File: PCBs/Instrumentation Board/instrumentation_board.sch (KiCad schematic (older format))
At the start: 24 parts, among them J1 Conn_01x02, J2 Conn_01x02, Q1 Q_Photo_NPN, U2 LSM6DS3HTR, U3 LSM6DS3HTR, U4 MicroSDBreakout, U5 GPS, U7 MS5607-02BA03

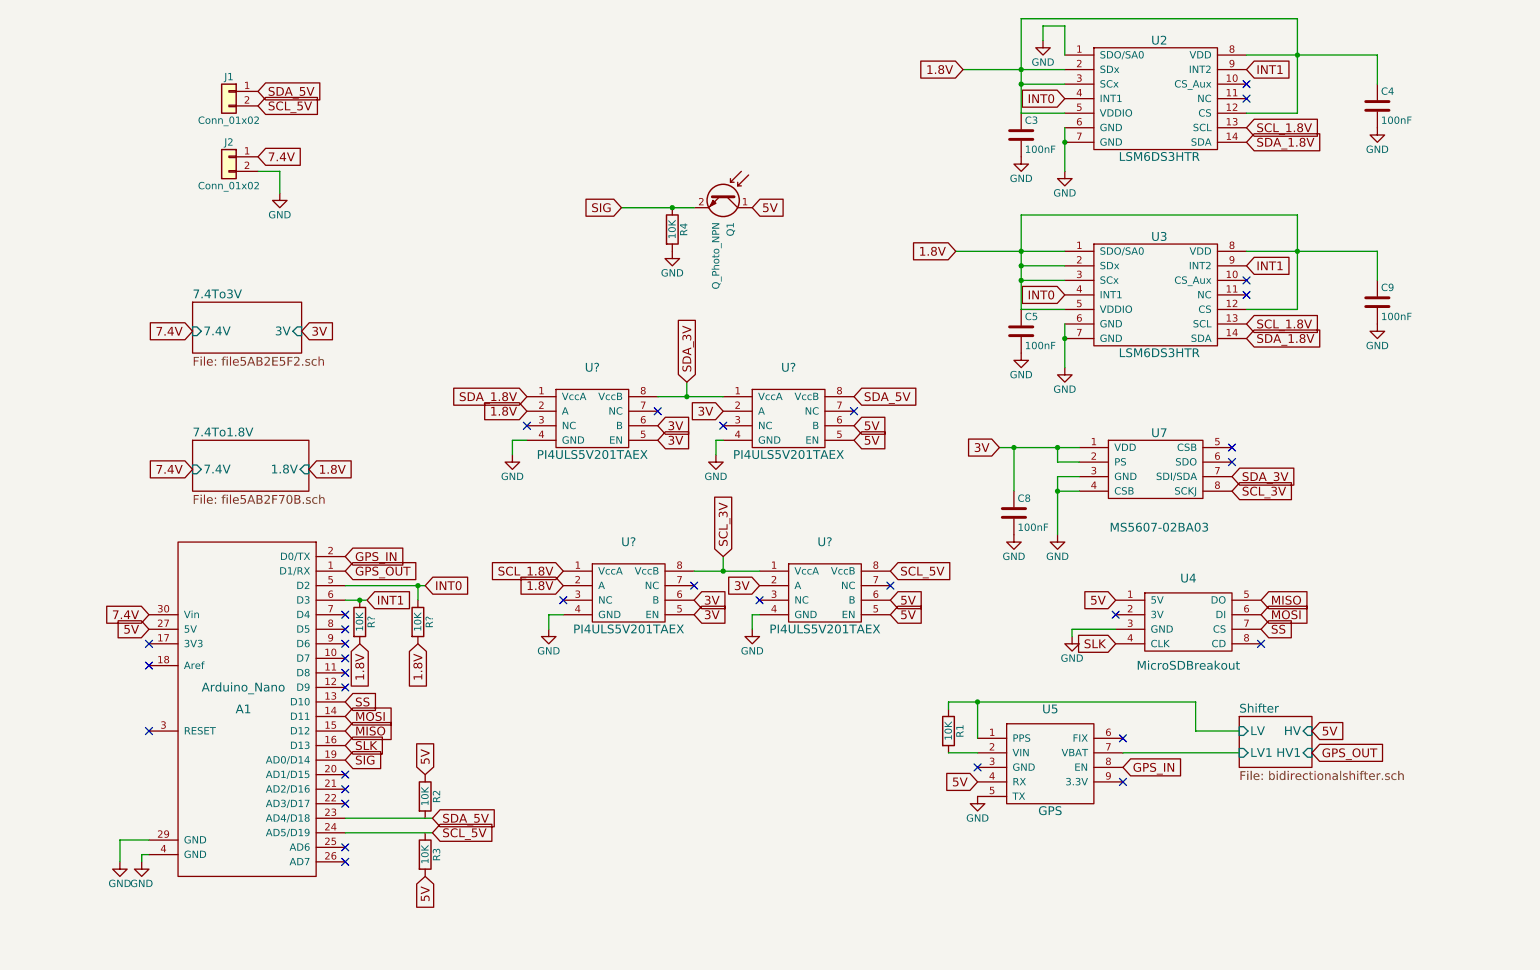
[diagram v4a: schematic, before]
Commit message: fixed swapped pins
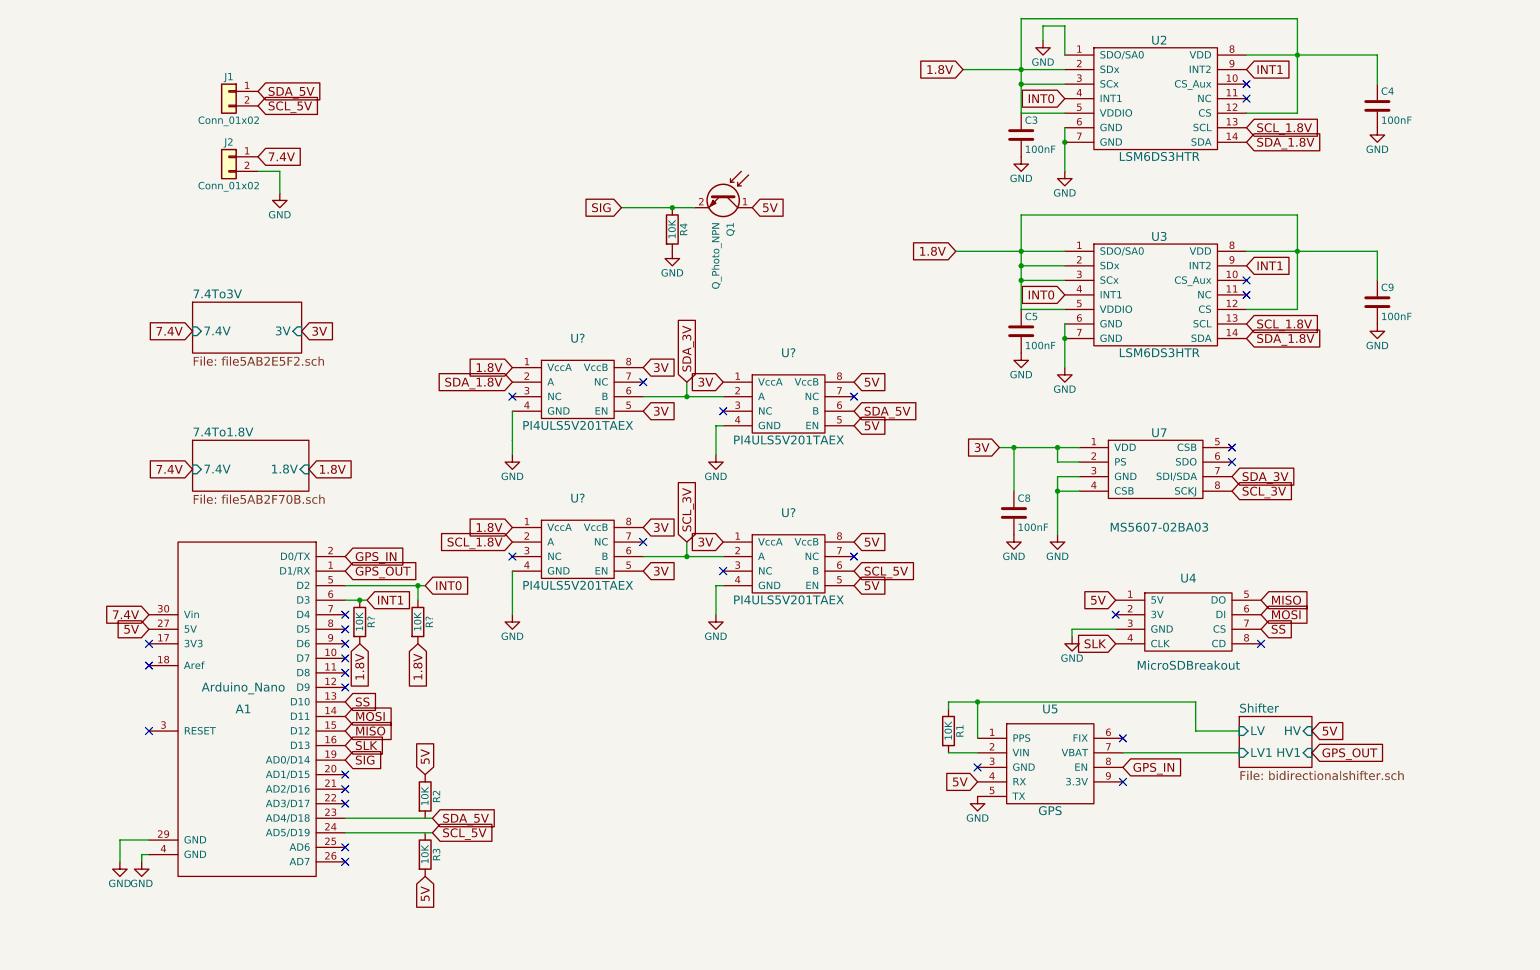
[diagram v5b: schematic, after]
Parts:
- removed U? (x2): PI4ULS5V201TAEX, symbol PI4ULS5V201TAEX
- added U? (x2): PI4ULS5V201TAEX, symbol PI4ULS5V201TAEX
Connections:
- net 1.8V: now also U?.1 (VccA), U?.1 (VccA); no longer U?.2 (A)
- net 3V: now also U?.1 (VccA), U?.8 (VccB), U?.1 (VccA), U?.5 (EN), U?.8 (VccB); no longer U?.2 (A), U?.6 (B)
- net 5V: now also U?.8 (VccB), U?.5 (EN), U?.8 (VccB); no longer U?.6 (B)
- net GND: now also U?.4 (GND), U?.4 (GND)
- net SCL_1.8V: now also U?.2 (A)
- net SCL_3V: now also U?.2 (A), U?.6 (B)
- net SCL_5V: now also U?.6 (B)
- net SDA_1.8V: now also U?.2 (A); no longer U?.1 (VccA)
- net SDA_3V: now also U?.2 (A), U?.6 (B); no longer U?.1 (VccA), U?.8 (VccB)
- net SDA_5V: now also U?.6 (B); no longer U?.8 (VccB)
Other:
- moved on the sheet: U?
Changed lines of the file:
@@
 L PI4ULS5V201TAEX U?
 U 1 1 5AB5D648
-P 5850 3750
-F 0 "U?" H 5850 4300 60  0000 C CNN
-F 1 "PI4ULS5V201TAEX" H 5850 3700 60  0000 C CNN
-F 2 "" H 5850 3750 60  0001 C CNN
-F 3 "" H 5850 3750 60  0001 C CNN
-	1    5850 3750
-	1    0    0    -1
-$EndComp
-Text GLabel 6300 3600 2    60   Input ~ 0
+P 5850 3650
+F 0 "U?" H 5850 4200 60  0000 C CNN
+F 1 "PI4ULS5V201TAEX" H 5850 3600 60  0000 C CNN
+F 2 "" H 5850 3650 60  0001 C CNN
+F 3 "" H 5850 3650 60  0001 C CNN
+	1    5850 3650
+	1    0    0    -1
+$EndComp
+Text GLabel 6300 3300 2    60   Input ~ 0
 5V
-Text GLabel 6300 3400 2    60   Input ~ 0
+Text GLabel 6300 3500 2    60   Input ~ 0
 SDA_5V
-Text GLabel 5400 3500 0    60   Input ~ 0
+Text GLabel 5400 3300 0    60   Input ~ 0
 3V
 Text GLabel 5150 3300 1    60   Input ~ 0
 SDA_3V
-Text GLabel 6300 3700 2    60   Input ~ 0
+Text GLabel 6300 3600 2    60   Input ~ 0
 5V
 $Comp
@@
 L PI4ULS5V201TAEX U?
 U 1 1 5AB67DF3
-P 4500 3750
-F 0 "U?" H 4500 4300 60  0000 C CNN
-F 1 "PI4ULS5V201TAEX" H 4500 3700 60  0000 C CNN
-F 2 "" H 4500 3750 60  0001 C CNN
-F 3 "" H 4500 3750 60  0001 C CNN
-	1    4500 3750
+P 4400 3550
+F 0 "U?" H 4400 4100 60  0000 C CNN
+F 1 "PI4ULS5V201TAEX" H 4400 3500 60  0000 C CNN
+F 2 "" H 4400 3550 60  0001 C CNN
+F 3 "" H 4400 3550 60  0001 C CNN
+	1    4400 3550
 	1    0    0    -1
 $EndComp
@@
 	7150 5500 7150 5750
 Wire Wire Line
-	6950 5500 8650 5500
-Wire Wire Line
-	7000 2400 7750 2400
+	6950 5500 7150 5500
+Wire Wire Line
+	7150 5500 8650 5500
+Wire Wire Line
+	7000 2400 7450 2400
+Wire Wire Line
+	7450 2400 7750 2400
 Wire Wire Line
 	7600 850  7600 950
@@
 Connection ~ 7750 3000
 Wire Wire Line
-	7750 2900 7750 3200
+	7750 2900 7750 3000
+Wire Wire Line
+	7750 3000 7750 3200
 Wire Wire Line
 	9350 2800 9000 2800
@@
 	7450 2800 7750 2800
 Wire Wire Line
-	9000 2400 9900 2400
-Wire Wire Line
-	9350 2150 9350 2800
+	9000 2400 9350 2400
+Wire Wire Line
+	9350 2400 9900 2400
+Wire Wire Line
+	9350 2150 9350 2400
+Wire Wire Line
+	9350 2400 9350 2800
 Wire Wire Line
 	7450 2150 9350 2150
 Wire Wire Line
-	7450 2150 7450 2800
+	7450 2150 7450 2400
+Wire Wire Line
+	7450 2400 7450 2500
+Wire Wire Line
+	7450 2500 7450 2600
+Wire Wire Line
+	7450 2600 7450 2800
 Connection ~ 7450 1250
 Wire Wire Line
@@
 Connection ~ 7450 1150
 Wire Wire Line
-	7050 1150 7750 1150
+	7050 1150 7450 1150
+Wire Wire Line
+	7450 1150 7750 1150
 Connection ~ 7750 1650
 Wire Wire Line
-	7750 1550 7750 1850
+	7750 1550 7750 1650
+Wire Wire Line
+	7750 1650 7750 1850
 Wire Wire Line
 	9350 1450 9000 1450
@@
 	7450 1450 7750 1450
 Wire Wire Line
-	9000 1050 9900 1050
-Wire Wire Line
-	9350 800  9350 1450
+	9000 1050 9350 1050
+Wire Wire Line
+	9350 1050 9900 1050
+Wire Wire Line
+	9350 800  9350 1050
+Wire Wire Line
+	9350 1050 9350 1450
 Wire Wire Line
 	7450 800  9350 800
 Wire Wire Line
-	7450 800  7450 1450
+	7450 800  7450 1150
+Wire Wire Line
+	7450 1150 7450 1250
+Wire Wire Line
+	7450 1250 7450 1450
 Wire Wire Line
 	7800 5000 8100 5000
@@
 	7850 4050 7700 4050
 Wire Wire Line
-	7700 3950 7700 4350
+	7700 3950 7700 4050
+Wire Wire Line
+	7700 4050 7700 4350
 Wire Wire Line
 	7850 3950 7700 3950
@@
 	7400 3750 7400 4050
 Wire Wire Line
-	7300 3750 7850 3750
+	7300 3750 7400 3750
+Wire Wire Line
+	7400 3750 7700 3750
+Wire Wire Line
+	7700 3750 7850 3750
 Wire Wire Line
 	1250 6450 1450 6450
@@
 	2800 6400 3400 6400
 Wire Wire Line
-	4700 2100 5200 2100
+	4700 2100 5050 2100
+Wire Wire Line
+	5050 2100 5200 2100
 Connection ~ 5050 2100
 Wire Wire Line
-	5350 3800 5350 3700
-Wire Wire Line
-	5350 3700 5400 3700
-Wire Wire Line
-	4950 3400 5400 3400
+	5350 3800 5350 3600
+Wire Wire Line
+	5350 3600 5400 3600
+Wire Wire Line
+	4850 3400 5150 3400
+Wire Wire Line
+	5150 3400 5400 3400
 Wire Wire Line
 	5150 3400 5150 3300
 Connection ~ 5150 3400
-NoConn ~ 6300 3500
-NoConn ~ 5400 3600
-Text GLabel 4950 3600 2    60   Input ~ 0
-3V
-Text GLabel 4950 3700 2    60   Input ~ 0
-3V
-NoConn ~ 4950 3500
-NoConn ~ 4050 3600
-Text GLabel 4050 3500 0    60   Input ~ 0
+NoConn ~ 6300 3400
+NoConn ~ 5400 3500
+Text GLabel 4850 3200 2    60   Input ~ 0
+3V
+Text GLabel 4850 3500 2    60   Input ~ 0
+3V
+NoConn ~ 4850 3300
+NoConn ~ 3950 3400
+Text GLabel 3950 3200 0    60   Input ~ 0
 1.8V
-Text GLabel 4050 3400 0    60   Input ~ 0
+Text GLabel 3950 3300 0    60   Input ~ 0
 SDA_1.8V
-$Comp
-L PI4ULS5V201TAEX U?
-U 1 1 5AB6A1B5
-P 6100 4950
-F 0 "U?" H 6100 5500 60  0000 C CNN
-F 1 "PI4ULS5V201TAEX" H 6100 4900 60  0000 C CNN
-F 2 "" H 6100 4950 60  0001 C CNN
-F 3 "" H 6100 4950 60  0001 C CNN
-	1    6100 4950
-	1    0    0    -1
-$EndComp
-Text GLabel 6550 4800 2    60   Input ~ 0
-5V
-Text GLabel 5650 4700 0    60   Input ~ 0
-3V
-Text GLabel 6550 4900 2    60   Input ~ 0
-5V
-$Comp
-L GND #PWR?
-U 1 1 5AB6A1C0
-P 5600 5000
-F 0 "#PWR?" H 5600 4750 50  0001 C CNN
-F 1 "GND" H 5600 4850 50  0000 C CNN
-F 2 "" H 5600 5000 50  0001 C CNN
-F 3 "" H 5600 5000 50  0001 C CNN
-	1    5600 5000
-	1    0    0    -1
-$EndComp
-$Comp
-L PI4ULS5V201TAEX U?
-U 1 1 5AB6A1C6
-P 4750 4950
-F 0 "U?" H 4750 5500 60  0000 C CNN
-F 1 "PI4ULS5V201TAEX" H 4750 4900 60  0000 C CNN
-F 2 "" H 4750 4950 60  0001 C CNN
-F 3 "" H 4750 4950 60  0001 C CNN
-	1    4750 4950
-	1    0    0    -1
-$EndComp
-Wire Wire Line
-	5600 5000 5600 4900
-Wire Wire Line
-	5600 4900 5650 4900
-Wire Wire Line
-	5200 4600 5650 4600
-Wire Wire Line
-	5400 4600 5400 4500
-Connection ~ 5400 4600
-NoConn ~ 6550 4700
-NoConn ~ 5650 4800
-Text GLabel 5200 4800 2    60   Input ~ 0
-3V
-Text GLabel 5200 4900 2    60   Input ~ 0
-3V
-NoConn ~ 5200 4700
-NoConn ~ 4300 4800
-Text GLabel 4300 4700 0    60   Input ~ 0
-1.8V
 $Comp
 L GND #PWR?
@@
 	1    0    0    -1
 $EndComp
-$Comp
-L GND #PWR?
-U 1 1 5AB6A36E
-P 4200 5000
-F 0 "#PWR?" H 4200 4750 50  0001 C CNN
-F 1 "GND" H 4200 4850 50  0000 C CNN
-F 2 "" H 4200 5000 50  0001 C CNN
-F 3 "" H 4200 5000 50  0001 C CNN
-	1    4200 5000
-	1    0    0    -1
-$EndComp
 Wire Wire Line
 	3950 3800 3950 3700
 Wire Wire Line
-	3950 3700 4050 3700
-Wire Wire Line
-	4200 5000 4200 4900
-Wire Wire Line
-	4200 4900 4300 4900
-Text GLabel 6550 4600 2    60   Input ~ 0
+	3950 3700 3950 3500
+Text GLabel 6300 4600 2    60   Input ~ 0
 SCL_5V
-Text GLabel 5400 4500 1    60   Input ~ 0
+Text GLabel 5150 4400 1    60   Input ~ 0
 SCL_3V
-Text GLabel 4300 4600 0    60   Input ~ 0
+Text GLabel 3950 4400 0    60   Input ~ 0
 SCL_1.8V
 Text GLabel 2900 5100 3    60   Input ~ 0
@@
 $EndComp
 Wire Wire Line
-	2800 4700 3350 4700
+	2800 4700 3300 4700
+Wire Wire Line
+	3300 4700 3350 4700
 Wire Wire Line
 	3300 4700 3300 4800
 Connection ~ 3300 4700
 Wire Wire Line
-	2800 4800 2950 4800
+	2800 4800 2900 4800
+Wire Wire Line
+	2900 4800 2950 4800
 Connection ~ 2900 4800
+$Comp
+L PI4ULS5V201TAEX U?
+U 1 1 5AB6EE1D
+P 5850 4750
+F 0 "U?" H 5850 5300 60  0000 C CNN
+F 1 "PI4ULS5V201TAEX" H 5850 4700 60  0000 C CNN
+F 2 "" H 5850 4750 60  0001 C CNN
+F 3 "" H 5850 4750 60  0001 C CNN
+	1    5850 4750
+	1    0    0    -1
+$EndComp
+Text GLabel 6300 4400 2    60   Input ~ 0
+5V
+Text GLabel 5400 4400 0    60   Input ~ 0
+3V
+Text GLabel 6300 4700 2    60   Input ~ 0
+5V
+$Comp
+L GND #PWR?
+U 1 1 5AB6EE28
+P 5350 4900
+F 0 "#PWR?" H 5350 4650 50  0001 C CNN
+F 1 "GND" H 5350 4750 50  0000 C CNN
+F 2 "" H 5350 4900 50  0001 C CNN
+F 3 "" H 5350 4900 50  0001 C CNN
+	1    5350 4900
+	1    0    0    -1
+$EndComp
+$Comp
+L PI4ULS5V201TAEX U?
+U 1 1 5AB6EE2E
+P 4400 4650
+F 0 "U?" H 4400 5200 60  0000 C CNN
+F 1 "PI4ULS5V201TAEX" H 4400 4600 60  0000 C CNN
+F 2 "" H 4400 4650 60  0001 C CNN
+F 3 "" H 4400 4650 60  0001 C CNN
+	1    4400 4650
+	1    0    0    -1
+$EndComp
+Wire Wire Line
+	5350 4900 5350 4700
+Wire Wire Line
+	5350 4700 5400 4700
+Wire Wire Line
+	4850 4500 5150 4500
+Wire Wire Line
+	5150 4500 5400 4500
+Wire Wire Line
+	5150 4500 5150 4400
+Connection ~ 5150 4500
+NoConn ~ 6300 4500
+NoConn ~ 5400 4600
+Text GLabel 4850 4300 2    60   Input ~ 0
+3V
+Text GLabel 4850 4600 2    60   Input ~ 0
+3V
+NoConn ~ 4850 4400
+NoConn ~ 3950 4500
+Text GLabel 3950 4300 0    60   Input ~ 0
+1.8V
+$Comp
+L GND #PWR?
+U 1 1 5AB6EE42
+P 3950 4900
+F 0 "#PWR?" H 3950 4650 50  0001 C CNN
+F 1 "GND" H 3950 4750 50  0000 C CNN
+F 2 "" H 3950 4900 50  0001 C CNN
+F 3 "" H 3950 4900 50  0001 C CNN
+	1    3950 4900
+	1    0    0    -1
+$EndComp
+Wire Wire Line
+	3950 4900 3950 4800
+Wire Wire Line
+	3950 4800 3950 4600
 $EndSCHEMATC

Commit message: changes as per Alex's review
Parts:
- removed R3, R? (x2): 10K, symbol R
- removed U? (x4): PI4ULS5V201TAEX, symbol PI4ULS5V201TAEX
- R1, R2: value 10K -> 0
- U4: value MicroSDBreakout -> MicroSD-ADAFRUIT254
- U5: value GPS -> GPS-ADAFRUIT746
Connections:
- net 5V: no longer R2.1
- net at R1.2: now also A1.5 (D2); no longer U5.2 (VIN)
- net at R2.2: now also A1.6 (D3)
- net INT0 renamed INT0_1.8V
- net INT0_1.8V: no longer A1.5 (D2)
- net INT1 renamed INT1_1.8V
- net INT1_1.8V: no longer A1.6 (D3)
- net Shifter/LV renamed ICShifter/VccA
- net ICShifter/VccA: no longer R1.1
- net Shifter/LV1 renamed ICShifter/A
- new net INT0_5V: R2.1
- new net INT1_5V: R1.1
- no-connect marks 33 -> 25
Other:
- moved on the sheet: C3, C5

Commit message: pinout changes
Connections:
- net 5V: now also U5.2 (VIN); no longer U5.4 (RX)
- net GND: now also U5.3 (GND); no longer U5.5 (TX)
- net GPS_IN: now also U5.4 (RX); no longer U5.8 (EN)
- net ICShifter/A: now also U5.5 (TX); no longer U5.7 (VBAT)
- net ICShifter/VccA: now also U5.9 (3.3V); no longer U5.1 (PPS)
- no-connect marks 25 -> 26
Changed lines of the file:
@@
 LIBS:contrib
 LIBS:valves
+LIBS:a2135-h
+LIBS:ap2204k-5
+LIBS:arduino_nano
+LIBS:fgpmmopa6h
+LIBS:Recovery Board Parts
+LIBS:Recovery Board-cache
+LIBS:sot-223
 LIBS:instrumentation_board_parts
 LIBS:instrumentation_board-cache
@@
 U 1 1 5A9B54D4
 P 7650 6000
-F 0 "U5" H 7650 6450 60  0000 C CNN
+F 0 "U5" H 7650 6500 60  0000 C CNN
 F 1 "GPS-ADAFRUIT746" H 7650 5750 60  0000 C CNN
 F 2 "" H 7750 5900 60  0001 C CNN
@@
 L GND #PWR5
 U 1 1 5A9B5B00
-P 7150 6150
-F 0 "#PWR5" H 7150 5900 50  0001 C CNN
-F 1 "GND" H 7150 6000 50  0000 C CNN
-F 2 "" H 7150 6150 50  0001 C CNN
-F 3 "" H 7150 6150 50  0001 C CNN
-	1    7150 6150
+P 6700 6100
+F 0 "#PWR5" H 6700 5850 50  0001 C CNN
+F 1 "GND" H 6700 5950 50  0000 C CNN
+F 2 "" H 6700 6100 50  0001 C CNN
+F 3 "" H 6700 6100 50  0001 C CNN
+	1    6700 6100
 	1    0    0    -1
 $EndComp
@@
 Text GLabel 2800 4600 2    60   Input ~ 0
 GPS_OUT
-Text GLabel 8150 5950 2    60   Input ~ 0
+Text GLabel 7150 6050 0    60   Input ~ 0
 GPS_IN
-Text GLabel 9650 5850 2    60   Input ~ 0
+Text GLabel 9650 6000 2    60   Input ~ 0
 GPS_OUT
 $Comp
@@
 Text GLabel 1450 5000 0    60   Input ~ 0
 5V
-Text GLabel 7150 6050 0    60   Input ~ 0
+Text GLabel 7150 5850 0    60   Input ~ 0
 5V
 Text GLabel 8100 4800 0    60   Input ~ 0
@@
 NoConn ~ 9100 5100
 NoConn ~ 8150 5750
-NoConn ~ 7150 5950
-NoConn ~ 8150 6050
 NoConn ~ 8900 3750
 NoConn ~ 8900 3850
@@
 F0 "ICShifter" 60
 F1 "Shifter.sch" 60
-F2 "B" I R 9650 5850 60
-F3 "VccB" I R 9650 6000 60
-F4 "A" I L 8950 5850 60
-F5 "VccA" I L 8950 6000 60
+F2 "B" I R 9650 6000 60
+F3 "VccB" I R 9650 5850 60
+F4 "A" I L 8950 6000 60
+F5 "VccA" I L 8950 5850 60
 $EndSheet
 $Sheet
@@
 	0    1    1    0
 $EndComp
-Text GLabel 9650 6000 2    60   Input ~ 0
+Text GLabel 9650 5850 2    60   Input ~ 0
 5V
 Connection ~ 7700 3750
@@
 	2800 4800 3100 4800
 Wire Wire Line
-	8150 5850 8950 5850
-Wire Wire Line
-	7150 5750 6850 5750
-Wire Wire Line
-	6850 5750 6850 6400
-Wire Wire Line
-	6850 6400 8750 6400
-Wire Wire Line
-	8750 6400 8750 6000
-Wire Wire Line
-	8750 6000 8950 6000
+	8600 5850 8950 5850
+Wire Wire Line
+	8600 5850 8600 6050
+Wire Wire Line
+	8600 6050 8150 6050
+NoConn ~ 8150 5950
+NoConn ~ 8150 5850
+Wire Wire Line
+	7150 5950 6700 5950
+Wire Wire Line
+	6700 5950 6700 6100
+Wire Wire Line
+	8950 6000 8850 6000
+Wire Wire Line
+	8850 6000 8850 6350
+Wire Wire Line
+	8850 6350 7000 6350
+Wire Wire Line
+	7000 6350 7000 6150
+Wire Wire Line
+	7000 6150 7150 6150
+NoConn ~ 7150 5750
 $EndSCHEMATC
